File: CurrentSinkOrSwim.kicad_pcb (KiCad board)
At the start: 2 copper layers, 41.7 x 48.5 mm, 22 parts, among them P1 HEATSINK, P101 CONN_01X02, P102 CONN_01X03, P103 CONN_01X02, Q401 BUK9575, U201 LMV358, U301 LM2931

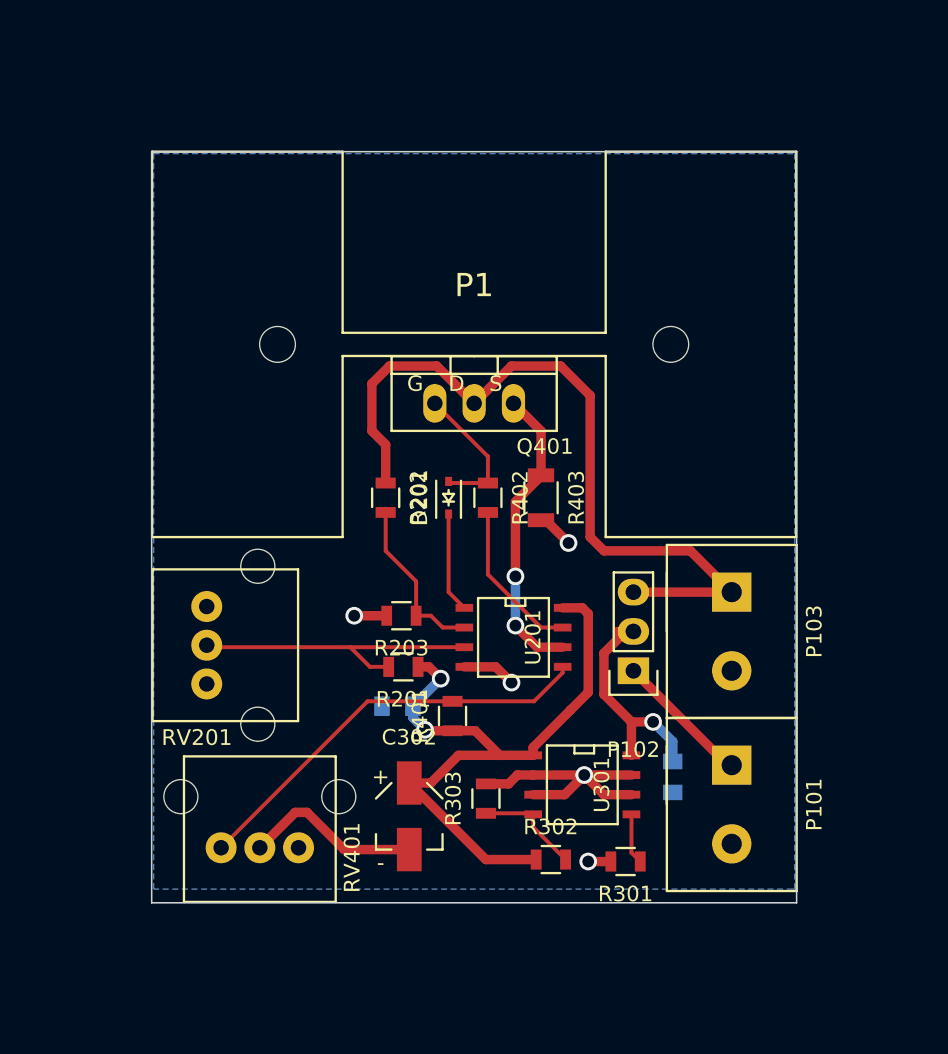
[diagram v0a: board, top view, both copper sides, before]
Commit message: updated sikscreen, shifted some components, enlarged ground plane, added mounting holes
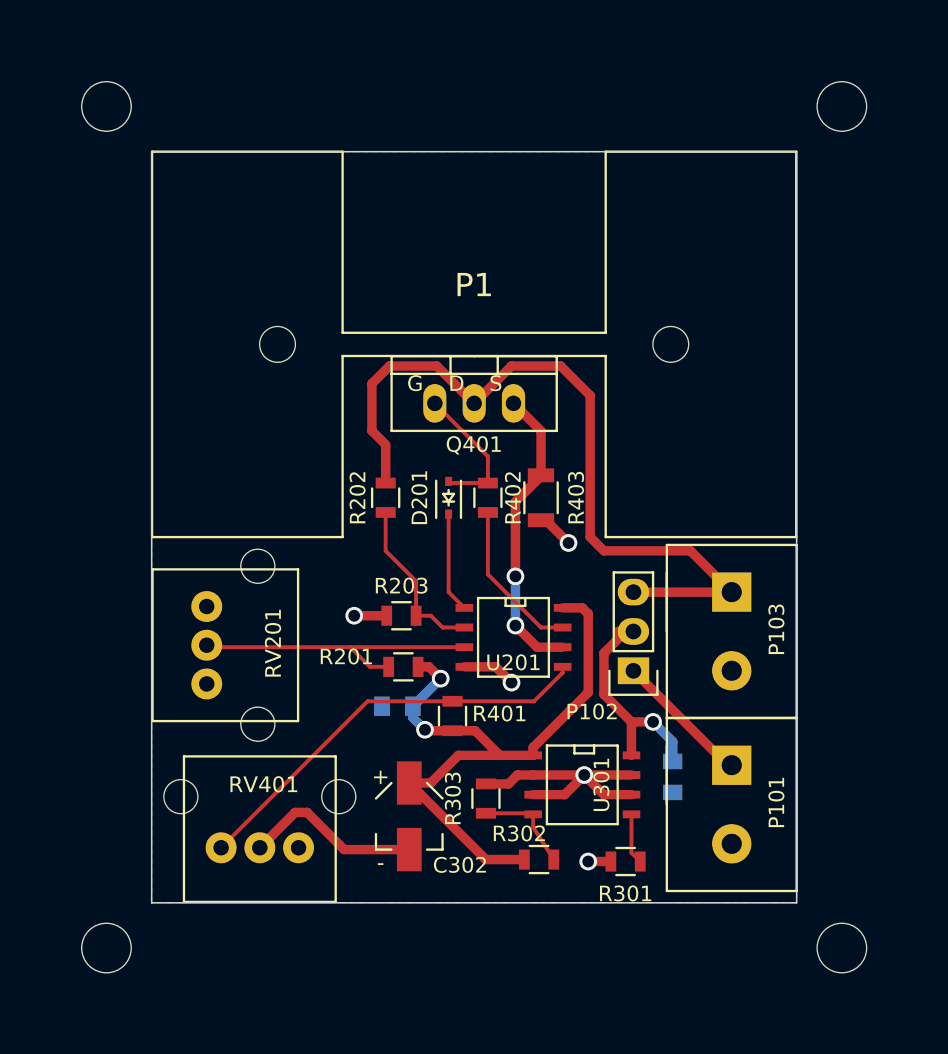
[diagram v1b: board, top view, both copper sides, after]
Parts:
- added REF**: MountingHole_3.2mm_M3, Mounting_Holes:MountingHole_3.2mm_M3, F.Cu at (150.7, 32.9)
- added REF**: MountingHole_3.2mm_M3, Mounting_Holes:MountingHole_3.2mm_M3, F.Cu at (103.3, 32.9)
- added REF**: MountingHole_3.2mm_M3, Mounting_Holes:MountingHole_3.2mm_M3, F.Cu at (150.7, 87.2)
- added REF**: MountingHole_3.2mm_M3, Mounting_Holes:MountingHole_3.2mm_M3, F.Cu at (103.3, 87.2)
- moved R302 0.76 mm to (131.2, 81.5)
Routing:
- net 2.7V: track 43.1 -> 42.3 mm
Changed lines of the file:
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@@
     (links 42)
     (no_connects 0)
-    (area 100.458199 35.434199 150.0508 90.041801)
+    (area 93.260057 27.2092 160.612943 92.5288)
     (thickness 1.6)
     (drawings 4)
     (tracks 119)
     (zones 0)
-    (modules 22)
+    (modules 26)
     (nets 17)
   )
@@
   (layers
     (0 F.Cu signal)
-    (31 B.Cu signal)
+    (31 B.Cu signal hide)
     (32 B.Adhes user)
     (33 F.Adhes user)
@@
     (descr "Through hole pin header")
     (tags "pin header")
-    (fp_text reference P103 (at 0 -5.334 270) (layer F.SilkS)
+    (fp_text reference P103 (at -0.127 -2.921 270) (layer F.SilkS)
       (effects (font (size 1 1) (thickness 0.15)))
     )
@@
     (tags "capacitor 0805")
     (attr smd)
-    (fp_text reference C201 (at 0 2.1 180) (layer B.SilkS)
+    (fp_text reference C201 (at 0.889 2.413 180) (layer B.SilkS)
       (effects (font (size 1 1) (thickness 0.15)) (justify mirror))
     )
@@
   (module Current:PCE3867CT-ND (layer F.Cu)
     (at 122.809 78.74 180)
-    (fp_text reference C302 (at 0 5.1 180) (layer F.SilkS)
+    (fp_text reference C302 (at -3.302 -3.175 180) (layer F.SilkS)
       (effects (font (size 1 1) (thickness 0.15)))
     )
@@
     (descr "Through hole pin header")
     (tags "pin header")
-    (fp_text reference P101 (at 0 -5.334 270) (layer F.SilkS)
+    (fp_text reference P101 (at -0.127 -2.921 270) (layer F.SilkS)
       (effects (font (size 1 1) (thickness 0.15)))
     )
@@
     (descr "Through hole pin header")
     (tags "pin header")
-    (fp_text reference P102 (at 0 -5.1 180) (layer F.SilkS)
+    (fp_text reference P102 (at 2.667 -2.667 180) (layer F.SilkS)
       (effects (font (size 1 1) (thickness 0.15)))
     )
@@
     (descr "TO-220, FET-GDS, Vertical,")
     (tags "TO-220, FET-GDS, Vertical,")
-    (fp_text reference Q401 (at 4.572 2.794) (layer F.SilkS)
+    (fp_text reference Q401 (at 0 2.667) (layer F.SilkS)
       (effects (font (size 1 1) (thickness 0.15)))
     )
@@
     (tags "resistor 0805")
     (attr smd)
-    (fp_text reference R201 (at 0 -2.1 180) (layer F.SilkS)
+    (fp_text reference R201 (at 3.683 0.635 180) (layer F.SilkS)
       (effects (font (size 1 1) (thickness 0.15)))
     )
@@
     (tags "resistor 0805")
     (attr smd)
-    (fp_text reference R202 (at 0 -2.1 270) (layer F.SilkS)
+    (fp_text reference R202 (at 0 1.778 270) (layer F.SilkS)
       (effects (font (size 1 1) (thickness 0.15)))
     )
@@
     (tags "resistor 0805")
     (attr smd)
-    (fp_text reference R203 (at 0 -2.1 180) (layer F.SilkS)
+    (fp_text reference R203 (at 0 1.905 180) (layer F.SilkS)
       (effects (font (size 1 1) (thickness 0.15)))
     )
@@
   )
   (module Resistors_SMD:R_0805 (layer F.Cu)
-    (at 131.953 81.534)
+    (at 131.191 81.534)
     (descr "Resistor SMD 0805, reflow soldering, Vishay (see dcrcw.pdf)")
     (tags "resistor 0805")
     (attr smd)
-    (fp_text reference R302 (at 0 -2.1) (layer F.SilkS)
+    (fp_text reference R302 (at -1.27 -1.651) (layer F.SilkS)
       (effects (font (size 1 1) (thickness 0.15)))
     )
@@
     (tags "resistor 0805")
     (attr smd)
-    (fp_text reference R401 (at 0 -2.1 90) (layer F.SilkS)
+    (fp_text reference R401 (at 0.127 3.048 180) (layer F.SilkS)
       (effects (font (size 1 1) (thickness 0.15)))
     )
@@
     (tags "resistor 0805")
     (attr smd)
-    (fp_text reference R402 (at 0 -2.1 270) (layer F.SilkS)
+    (fp_text reference R402 (at 0 -1.651 270) (layer F.SilkS)
       (effects (font (size 1 1) (thickness 0.15)))
     )
@@
   (module Current:P090L-02F25BR10K (layer F.Cu)
     (at 109.728 67.691 270)
-    (fp_text reference RV201 (at 5.969 0.635 360) (layer F.SilkS)
+    (fp_text reference RV201 (at -0.127 -4.318 450) (layer F.SilkS)
       (effects (font (size 1.016 1.016) (thickness 0.15)))
     )
@@
   (module Current:P090L-02F25BR10K (layer F.Cu)
     (at 113.157 80.772)
-    (fp_text reference RV401 (at 5.969 0.635 90) (layer F.SilkS)
+    (fp_text reference RV401 (at 0.254 -4.064 180) (layer F.SilkS)
       (effects (font (size 1.016 1.016) (thickness 0.15)))
     )
@@
     (tags "CMS SOJ")
     (attr smd)
-    (fp_text reference U201 (at 0 -1.27 270) (layer F.SilkS)
+    (fp_text reference U201 (at 1.651 0 360) (layer F.SilkS)
       (effects (font (size 1 1) (thickness 0.15)))
     )
@@
       (rotate (xyz 0 0 0))
     )
+  )
+  (module Mounting_Holes:MountingHole_3.2mm_M3 (layer F.Cu)
+    (at 150.749 32.893)
+    (descr "Mounting Hole 3.2mm, no annular, M3")
+    (tags "mounting hole 3.2mm no annular m3")
+    (fp_text reference REF** (at 0 -4.2) (layer F.SilkS) hide
+      (effects (font (size 1 1) (thickness 0.15)))
+    )
+    (fp_text value MountingHole_3.2mm_M3 (at 0 4.2) (layer F.Fab)
+      (effects (font (size 1 1) (thickness 0.15)))
+    )
+    (fp_circle (center 0 0) (end 3.2 0) (layer Cmts.User) (width 0.15))
+    (fp_circle (center 0 0) (end 3.45 0) (layer F.CrtYd) (width 0.05))
+    (pad 1 np_thru_hole circle (at 0 0) (size 3.2 3.2) (drill 3.2) (layers *.Cu *.Mask F.SilkS))
+  )
+  (module Mounting_Holes:MountingHole_3.2mm_M3 (layer F.Cu)
+    (at 103.251 32.893)
+    (descr "Mounting Hole 3.2mm, no annular, M3")
+    (tags "mounting hole 3.2mm no annular m3")
+    (fp_text reference REF** (at 0 -4.2) (layer F.SilkS) hide
+      (effects (font (size 1 1) (thickness 0.15)))
+    )
+    (fp_text value MountingHole_3.2mm_M3 (at 0 4.2) (layer F.Fab)
+      (effects (font (size 1 1) (thickness 0.15)))
+    )
+    (fp_circle (center 0 0) (end 3.2 0) (layer Cmts.User) (width 0.15))
+    (fp_circle (center 0 0) (end 3.45 0) (layer F.CrtYd) (width 0.05))
+    (pad 1 np_thru_hole circle (at 0 0) (size 3.2 3.2) (drill 3.2) (layers *.Cu *.Mask F.SilkS))
+  )
+  (module Mounting_Holes:MountingHole_3.2mm_M3 (layer F.Cu)
+    (at 150.749 87.249)
+    (descr "Mounting Hole 3.2mm, no annular, M3")
+    (tags "mounting hole 3.2mm no annular m3")
+    (fp_text reference REF** (at 0 -4.2) (layer F.SilkS) hide
+      (effects (font (size 1 1) (thickness 0.15)))
+    )
+    (fp_text value MountingHole_3.2mm_M3 (at 0 4.2) (layer F.Fab)
+      (effects (font (size 1 1) (thickness 0.15)))
+    )
+    (fp_circle (center 0 0) (end 3.2 0) (layer Cmts.User) (width 0.15))
+    (fp_circle (center 0 0) (end 3.45 0) (layer F.CrtYd) (width 0.05))
+    (pad 1 np_thru_hole circle (at 0 0) (size 3.2 3.2) (drill 3.2) (layers *.Cu *.Mask F.SilkS))
+  )
+  (module Mounting_Holes:MountingHole_3.2mm_M3 (layer F.Cu)
+    (at 103.251 87.249)
+    (descr "Mounting Hole 3.2mm, no annular, M3")
+    (tags "mounting hole 3.2mm no annular m3")
+    (fp_text reference REF** (at 0 -4.2) (layer F.SilkS) hide
+      (effects (font (size 1 1) (thickness 0.15)))
+    )
+    (fp_text value MountingHole_3.2mm_M3 (at 0 4.2) (layer F.Fab)
+      (effects (font (size 1 1) (thickness 0.15)))
+    )
+    (fp_circle (center 0 0) (end 3.2 0) (layer Cmts.User) (width 0.15))
+    (fp_circle (center 0 0) (end 3.45 0) (layer F.CrtYd) (width 0.05))
+    (pad 1 np_thru_hole circle (at 0 0) (size 3.2 3.2) (drill 3.2) (layers *.Cu *.Mask F.SilkS))
   )
   (gr_line (start 147.828 35.814) (end 106.172 35.814) (angle 90) (layer Edge.Cuts) (width 0.1))
@@
   (segment (start 134.366 65.659) (end 133.985 65.278) (width 0.6096) (layer F.Cu) (net 1))
   (segment (start 133.985 65.278) (end 132.715 65.278) (width 0.6096) (layer F.Cu) (net 1))
-  (segment (start 131.003 81.534) (end 127.753 81.534) (width 0.6096) (layer F.Cu) (net 1))
+  (segment (start 130.241 81.534) (end 127.753 81.534) (width 0.6096) (layer F.Cu) (net 1) (status 10))
   (segment (start 127.753 81.534) (end 122.809 76.59) (width 0.6096) (layer F.Cu) (net 1))
   (segment (start 135.829 81.661) (end 134.366 81.661) (width 0.6096) (layer F.Cu) (net 2))
@@
   (segment (start 130.744 78.547) (end 130.81 78.613) (width 0.254) (layer F.Cu) (net 12))
   (segment (start 130.81 78.613) (end 130.81 79.441) (width 0.254) (layer F.Cu) (net 12))
-  (segment (start 130.81 79.441) (end 132.903 81.534) (width 0.254) (layer F.Cu) (net 12))
+  (segment (start 130.81 79.441) (end 132.141 81.534) (width 0.254) (layer F.Cu) (net 12) (status 20))
   (segment (start 125.603 71.313) (end 120.116 71.313) (width 0.254) (layer F.Cu) (net 13))
   (segment (start 120.116 71.313) (end 110.657 80.772) (width 0.254) (layer F.Cu) (net 13))
@@
     (polygon
       (pts
-        (xy 147.574 83.439) (xy 106.299 83.439) (xy 106.299 35.941) (xy 147.701 35.941) (xy 147.701 83.439)
-        (xy 147.574 83.439)
+        (xy 147.828 84.328) (xy 106.172 84.328) (xy 106.172 35.814) (xy 147.828 35.814) (xy 147.828 84.328)
       )
     )
